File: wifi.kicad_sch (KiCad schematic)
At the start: 25 parts, among them P2 USB_C_Receptacle_USB2.0_16P, Q1 2N7002, Q2 2N7002, U7 SC16C550BIBS, U8 ESP32-C3-WROOM-02, Y1 24 MHz

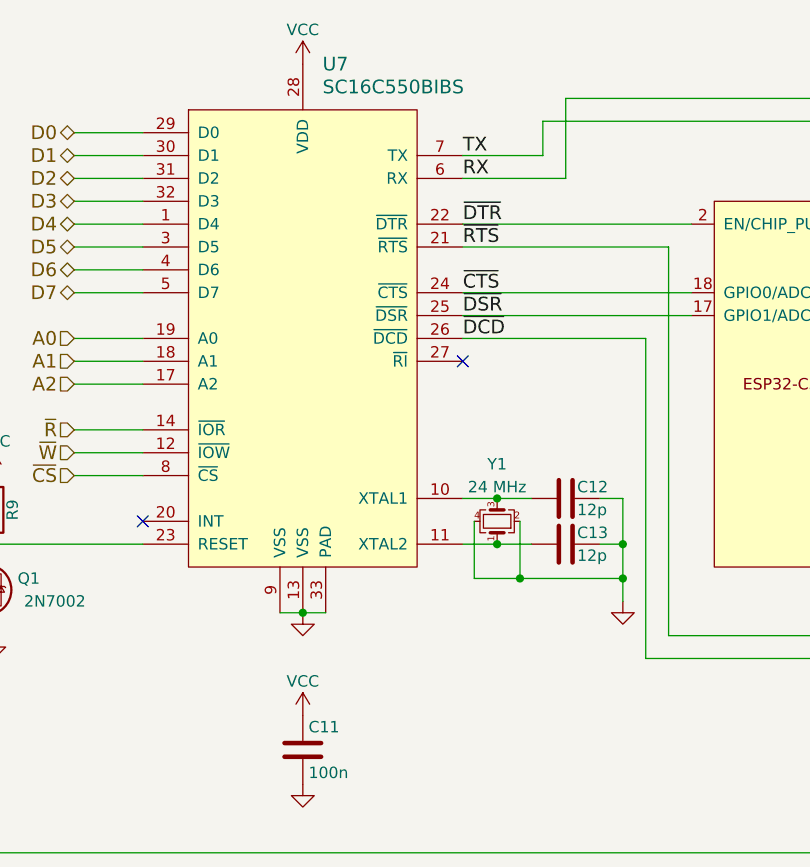
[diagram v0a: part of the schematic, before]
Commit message: Rev.C: replace SC16C550BIBS with TI TL16C550DRHB
The NXP SC16C550BIBS is out of stock everywhere. The TI TL16C550D in the
RHB (5x5 VQFN-32) package is pin-for-pin compatible and register
compatible (auto RTS/CTS via MCR AFE), so the existing driver works.

- U7: TL16C550DRHB (LCSC C2653239), Texas RHB0032E footprint (EP 3.45 mm,
  perimeter pads unchanged); pin names updated to TI naming.
- Y1: 20 MHz crystal (TXC 7E20000E12UCG, C252261, 12 pF load). TI rates
  the RHB package to 20 MHz at 3.3 V, so the UART link runs at
  1.25 Mbaud (divisor 1). SGDK 16c550.h and mw-fw-rtos LSD_UART_BR must
  be set to match; existing ROMs/firmware at 1.5 Mbaud will not work.
- R18: 1 MOhm oscillator bias resistor across XIN/XOUT (C26083); the TI
  oscillator has no internal Rp, unlike the NXP part.
- RI (pin 27) tied to VCC; the TI part has no internal modem-input
  pull-ups.
- XIN/XOUT nets are now labelled (/WiFi/XIN, /WiFi/XOUT).
- Zones refilled.
- Revision bumped to Rev.C (title blocks and silkscreen), credits
  doragasu 2024, jfryman 2026.

Files remain in KiCad 8 format.

Co-Authored-By: Claude Opus 5.5 <noreply@anthropic.com>
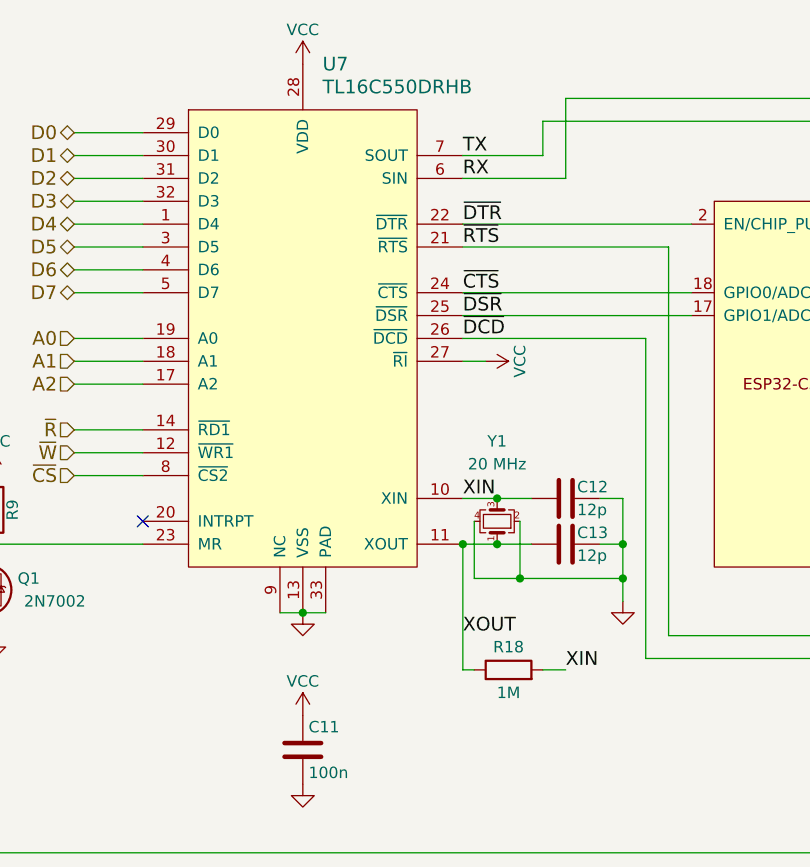
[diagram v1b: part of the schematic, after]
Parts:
- added R18: 1M, Resistor_SMD:R_0402_1005Metric, symbol Device:R
- U7: value SC16C550BIBS -> TL16C550DRHB; footprint Package_DFN_QFN:HVQFN-32-1EP_5x5mm_P0.5mm_EP3.1x3.1mm -> Package_DFN_QFN:Texas_RHB0032E_VQFN-32-1EP_5x5mm_P0.5mm_EP3.45x3.45mm; symbol doragasu:SC16C550BIBS -> mw-cart:TL16C550DRHB; LCSC# C3310482 -> C2653239; manf# (none) -> TL16C550DRHBR
- Y1: value 24 MHz -> 20 MHz; LCSC# C2901723 -> C252261; manf# (none) -> 7E20000E12UCG
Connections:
- net VCC: now also U7.27 (~{RI})
- net XIN: now reaches C12.2, U7.10 (XIN), Y1.3
- net XIN: now also R18.2
- net XOUT: now reaches C13.2, U7.11 (XOUT), Y1.1
- net XOUT: now also R18.1
- no-connect marks 4 -> 3
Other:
- company: doragasu -> doragasu, jfryman
